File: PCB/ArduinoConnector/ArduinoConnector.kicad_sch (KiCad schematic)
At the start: 6 parts, among them J1 Ard1, J2 Ard2, J3 FAN, Q1 MMBT100

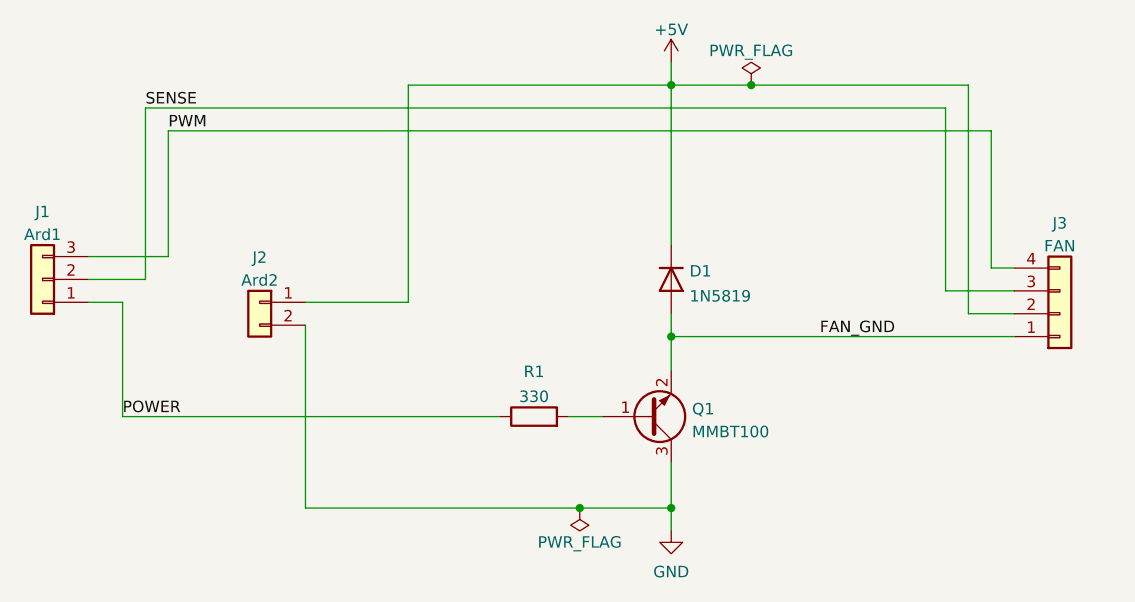
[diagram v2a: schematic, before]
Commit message: New version of the ArduinoConnector
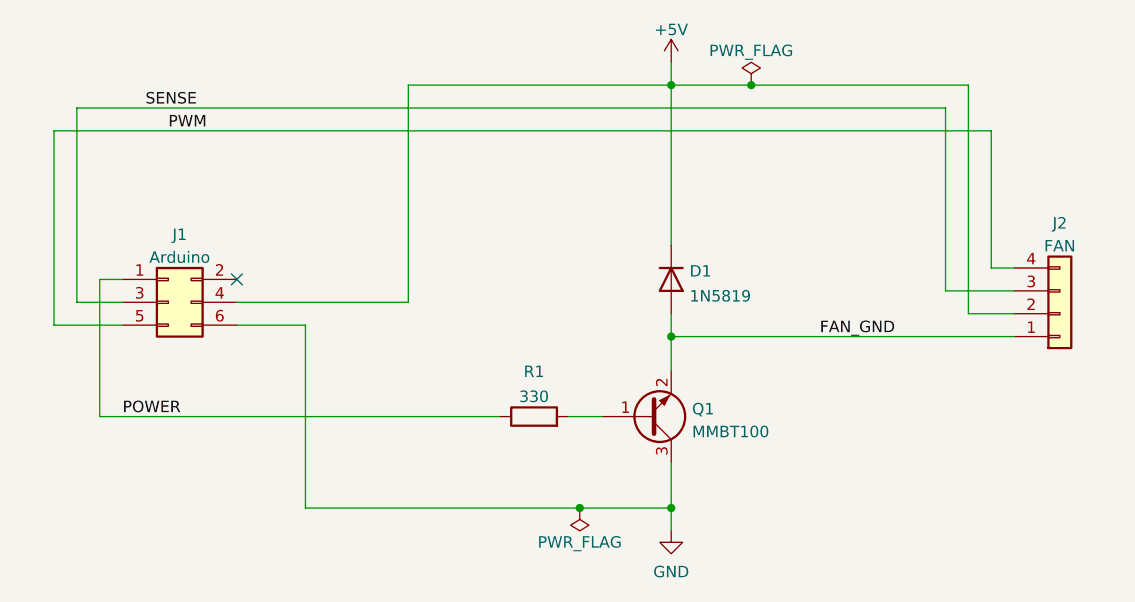
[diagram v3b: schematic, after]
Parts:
- removed J1: Ard1, Connector_PinHeader_2.54mm:PinHeader_1x03_P2.54mm_Vertical, symbol Connector_Generic:Conn_01x03
- removed J2: Ard2, Connector_PinHeader_2.54mm:PinHeader_1x02_P2.54mm_Vertical, symbol Connector_Generic:Conn_01x02
- added J1: Arduino, Connector_PinHeader_2.54mm:PinHeader_2x03_P2.54mm_Vertical, symbol Connector_Generic:Conn_02x03_Odd_Even
- renumbered J3 to J2
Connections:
- net +5V: now also J1.4 (Pin_4)
- net GND: now also J1.6 (Pin_6)
- net POWER: now also J1.1 (Pin_1)
- net PWM: now also J1.5 (Pin_5)
- net SENSE: now also J1.3 (Pin_3)
- no-connect marks 0 -> 1
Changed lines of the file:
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@@
   (junction (at 137.16 90.17) (diameter 0) (color 0 0 0 0)
   )
+  (no_connect (at 88.9 83.82))
   (wire (pts (xy 96.52 109.22) (xy 127 109.22))
     (stroke (width 0) (type default) (color 0 0 0 0))
   )
-  (wire (pts (xy 72.39 81.28) (xy 81.28 81.28))
-    (stroke (width 0) (type default) (color 0 0 0 0))
-  )
-  (wire (pts (xy 72.39 86.36) (xy 76.2 86.36))
-    (stroke (width 0) (type default) (color 0 0 0 0))
-  )
   (wire (pts (xy 96.52 88.9) (xy 96.52 109.22))
     (stroke (width 0) (type default) (color 0 0 0 0))
@@
     (stroke (width 0) (type default) (color 0 0 0 0))
   )
-  (wire (pts (xy 76.2 86.36) (xy 76.2 99.06))
+  (wire (pts (xy 88.9 88.9) (xy 96.52 88.9))
+    (stroke (width 0) (type default) (color 0 0 0 0))
+  )
+  (wire (pts (xy 76.2 86.36) (xy 71.12 86.36))
     (stroke (width 0) (type default) (color 0 0 0 0))
   )
@@
     (stroke (width 0) (type default) (color 0 0 0 0))
   )
-  (wire (pts (xy 76.2 99.06) (xy 118.11 99.06))
-    (stroke (width 0) (type default) (color 0 0 0 0))
-  )
-  (wire (pts (xy 78.74 64.77) (xy 167.64 64.77))
+  (wire (pts (xy 73.66 99.06) (xy 118.11 99.06))
+    (stroke (width 0) (type default) (color 0 0 0 0))
+  )
+  (wire (pts (xy 76.2 83.82) (xy 73.66 83.82))
+    (stroke (width 0) (type default) (color 0 0 0 0))
+  )
+  (wire (pts (xy 71.12 64.77) (xy 167.64 64.77))
+    (stroke (width 0) (type default) (color 0 0 0 0))
+  )
+  (wire (pts (xy 76.2 88.9) (xy 68.58 88.9))
     (stroke (width 0) (type default) (color 0 0 0 0))
   )
@@
     (stroke (width 0) (type default) (color 0 0 0 0))
   )
-  (wire (pts (xy 96.52 86.36) (xy 107.95 86.36))
+  (wire (pts (xy 88.9 86.36) (xy 107.95 86.36))
     (stroke (width 0) (type default) (color 0 0 0 0))
   )
@@
     (stroke (width 0) (type default) (color 0 0 0 0))
   )
-  (wire (pts (xy 78.74 64.77) (xy 78.74 83.82))
-    (stroke (width 0) (type default) (color 0 0 0 0))
-  )
-  (wire (pts (xy 72.39 83.82) (xy 78.74 83.82))
+  (wire (pts (xy 73.66 83.82) (xy 73.66 99.06))
+    (stroke (width 0) (type default) (color 0 0 0 0))
+  )
+  (wire (pts (xy 71.12 86.36) (xy 71.12 64.77))
     (stroke (width 0) (type default) (color 0 0 0 0))
   )
@@
     (stroke (width 0) (type default) (color 0 0 0 0))
   )
-  (wire (pts (xy 81.28 81.28) (xy 81.28 67.31))
-    (stroke (width 0) (type default) (color 0 0 0 0))
-  )
   (wire (pts (xy 137.16 90.17) (xy 137.16 93.98))
     (stroke (width 0) (type default) (color 0 0 0 0))
   )
-  (wire (pts (xy 81.28 67.31) (xy 172.72 67.31))
+  (wire (pts (xy 68.58 67.31) (xy 172.72 67.31))
     (stroke (width 0) (type default) (color 0 0 0 0))
   )
@@
   )
   (wire (pts (xy 107.95 62.23) (xy 137.16 62.23))
+    (stroke (width 0) (type default) (color 0 0 0 0))
+  )
+  (wire (pts (xy 68.58 88.9) (xy 68.58 67.31))
     (stroke (width 0) (type default) (color 0 0 0 0))
   )
@@
     (pin "2")
   )
-  (symbol (lib_id "Connector_Generic:Conn_01x02") (at 91.44 86.36 0) (mirror y) (unit 1)
-    (in_bom yes) (on_board yes) (fields_autoplaced)
-    (property "Reference" "J2" (id 0) (at 91.44 81.3902 0))
-    (property "Value" "Ard2" (id 1) (at 91.44 83.9271 0))
-    (property "Footprint" "Connector_PinHeader_2.54mm:PinHeader_1x02_P2.54mm_Vertical" (id 2) (at 91.44 86.36 0)
-      (effects (font (size 1.27 1.27)) hide)
-    )
-    (property "Datasheet" "~" (id 3) (at 91.44 86.36 0)
-      (effects (font (size 1.27 1.27)) hide)
-    )
-    (pin "1")
-    (pin "2")
-  )
   (symbol (lib_id "power:PWR_FLAG") (at 146.05 62.23 0) (mirror y) (unit 1)
     (in_bom yes) (on_board yes)
@@
     (pin "1")
   )
-  (symbol (lib_id "Connector_Generic:Conn_01x03") (at 67.31 83.82 180) (unit 1)
-    (in_bom yes) (on_board yes) (fields_autoplaced)
-    (property "Reference" "J1" (id 0) (at 67.31 76.3102 0))
-    (property "Value" "Ard1" (id 1) (at 67.31 78.8471 0))
-    (property "Footprint" "Connector_PinHeader_2.54mm:PinHeader_1x03_P2.54mm_Vertical" (id 2) (at 67.31 83.82 0)
-      (effects (font (size 1.27 1.27)) hide)
-    )
-    (property "Datasheet" "~" (id 3) (at 67.31 83.82 0)
-      (effects (font (size 1.27 1.27)) hide)
-    )
-    (pin "1")
-    (pin "2")
-    (pin "3")
-  )
   (symbol (lib_id "Connector_Generic:Conn_01x04") (at 180.34 87.63 0) (mirror x) (unit 1)
     (in_bom yes) (on_board yes) (fields_autoplaced)
-    (property "Reference" "J3" (id 0) (at 180.34 77.5802 0))
+    (property "Reference" "J2" (id 0) (at 180.34 77.5802 0))
     (property "Value" "FAN" (id 1) (at 180.34 80.1171 0))
     (property "Footprint" "Connector_Molex:Molex_KK-254_AE-6410-04A_1x04_P2.54mm_Vertical" (id 2) (at 180.34 87.63 0)
@@
     (pin "2")
     (pin "3")
+  )
+  (symbol (lib_id "Connector_Generic:Conn_02x03_Odd_Even") (at 81.28 86.36 0) (unit 1)
+    (in_bom yes) (on_board yes) (fields_autoplaced)
+    (property "Reference" "J1" (id 0) (at 82.55 78.8502 0))
+    (property "Value" "Arduino" (id 1) (at 82.55 81.3871 0))
+    (property "Footprint" "Connector_PinHeader_2.54mm:PinHeader_2x03_P2.54mm_Vertical" (id 2) (at 81.28 86.36 0)
+      (effects (font (size 1.27 1.27)) hide)
+    )
+    (property "Datasheet" "~" (id 3) (at 81.28 86.36 0)
+      (effects (font (size 1.27 1.27)) hide)
+    )
+    (pin "1")
+    (pin "2")
+    (pin "3")
+    (pin "4")
+    (pin "5")
+    (pin "6")
   )
   (symbol (lib_id "power:PWR_FLAG") (at 127 109.22 180) (unit 1)
@@
       (reference "D1") (unit 1) (value "1N5819") (footprint "Diode_SMD:D_SMA")
     )
-    (path "/888c6fdf-c198-440a-97af-035b863dc875"
-      (reference "J1") (unit 1) (value "Ard1") (footprint "Connector_PinHeader_2.54mm:PinHeader_1x03_P2.54mm_Vertical")
-    )
-    (path "/55b28997-b330-40d1-b32a-125cd071668d"
-      (reference "J2") (unit 1) (value "Ard2") (footprint "Connector_PinHeader_2.54mm:PinHeader_1x02_P2.54mm_Vertical")
+    (path "/a9240eb1-cd96-4728-9dbf-17ea5e90b45d"
+      (reference "J1") (unit 1) (value "Arduino") (footprint "Connector_PinHeader_2.54mm:PinHeader_2x03_P2.54mm_Vertical")
     )
     (path "/9661476a-e3cc-43ad-bbdf-24b6874ef400"
-      (reference "J3") (unit 1) (value "FAN") (footprint "Connector_Molex:Molex_KK-254_AE-6410-04A_1x04_P2.54mm_Vertical")
+      (reference "J2") (unit 1) (value "FAN") (footprint "Connector_Molex:Molex_KK-254_AE-6410-04A_1x04_P2.54mm_Vertical")
     )
     (path "/a83bc339-0e58-46db-b9d7-1089d0fbf78b"
